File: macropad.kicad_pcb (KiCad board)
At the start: 2 copper layers, 13 parts, among them SW1 Rotary_Encoder_Switch, SW2 Rotary_Encoder_Switch, SW3 Rotary_Encoder_Switch, SW4 Rotary_Encoder_Switch, SW5 Rotary_Encoder_Switch, SW6 Rotary_Encoder_Switch, U1 ProMicro

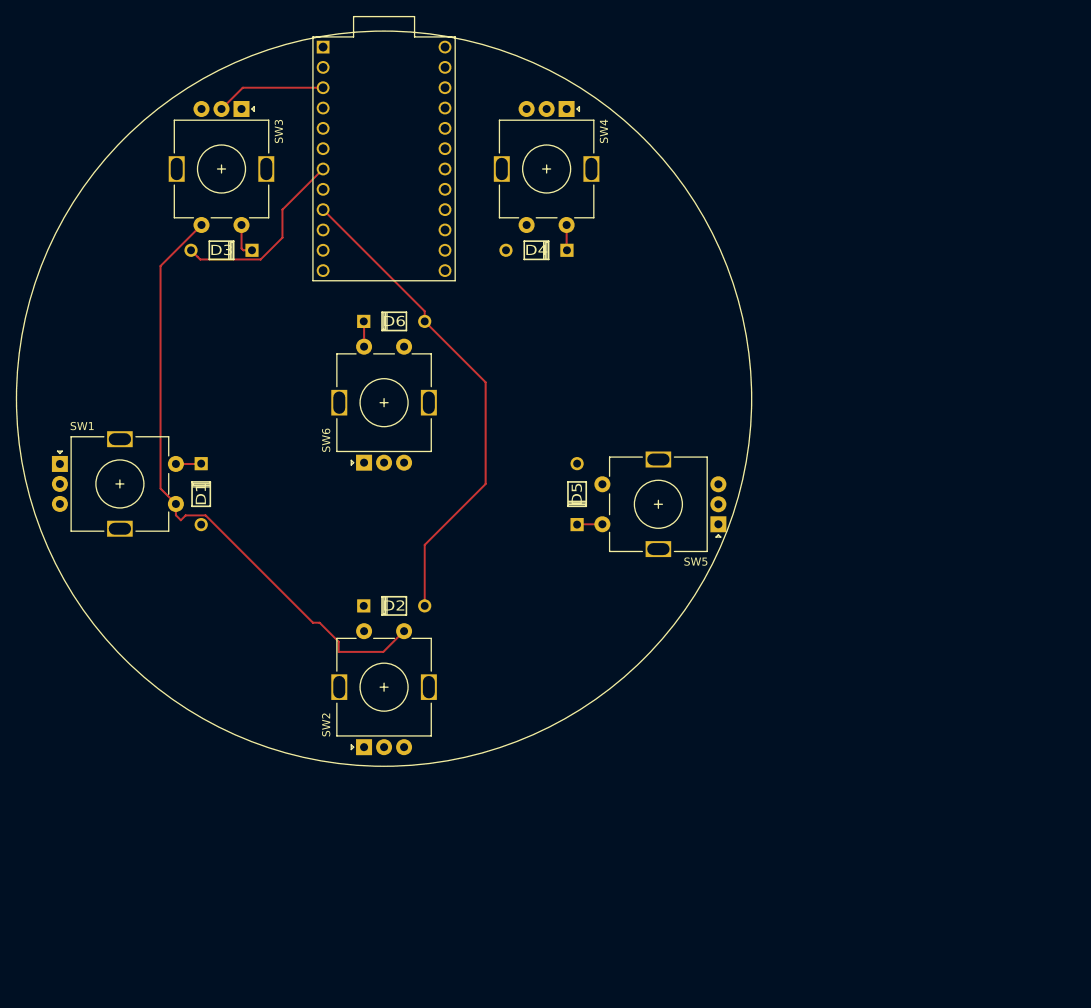
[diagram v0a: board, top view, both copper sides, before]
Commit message: moved to 70mm circle, just before routing
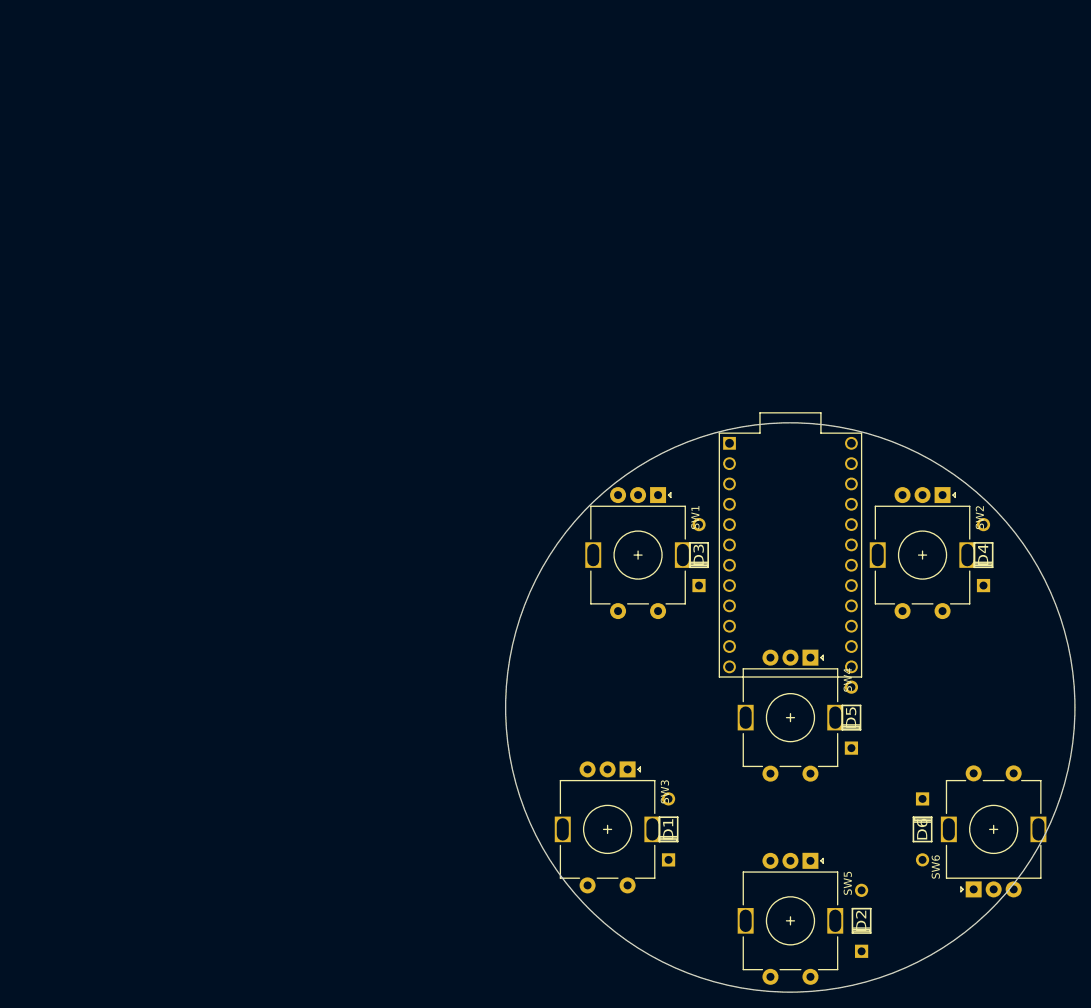
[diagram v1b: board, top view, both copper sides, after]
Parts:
- moved SW6 93.0 mm to (175.3, 118.1)
- moved D6 91.6 mm to (166.4, 118.1), turned to 90 degrees
- moved SW3 74.7 mm to (127.0, 118.1), turned to 270 degrees
- moved D1 71.9 mm to (134.6, 118.1), turned to 270 degrees
- moved SW1 71.0 mm to (130.8, 83.8)
- moved U1 70.9 mm to (149.9, 83.8)
- moved D3 70.8 mm to (138.4, 83.8), turned to 270 degrees
- moved D2 70.4 mm to (158.8, 129.5), turned to 270 degrees
- moved D4 67.6 mm to (174.0, 83.8), turned to 270 degrees
- moved SW2 67.4 mm to (166.4, 83.8)
- moved SW5 58.6 mm to (149.9, 129.5), turned to 270 degrees
- moved D5 44.2 mm to (157.5, 104.1)
- moved SW4 31.4 mm to (149.9, 104.1), turned to 270 degrees
- renumbered SW3 to SW1, SW4 to SW2, SW1 to SW3, SW5 to SW4, SW2 to SW5
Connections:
- U1 pad 1: RE4-0 -> RE0-0
- U1 pad 19: RE0-1 -> RE4-1
- U1 pad 2: RE4-1 -> RE0-1
- U1 pad 20: RE0-0 -> RE4-0
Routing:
- net Net-(SW1-PadS1): track 77.1 -> 0.00 mm
- net ROW2: track 61.1 -> 0.00 mm
- net ROW0: track 23.7 -> 0.00 mm
- net GND: track 13.8 -> 0.00 mm
- net Net-(D3-Pad2): track 4.33 -> 0.00 mm
- net Net-(D4-Pad2): track 3.18 -> 0.00 mm
- net Net-(D5-Pad2): track 3.18 -> 0.00 mm
- net Net-(D6-Pad2): track 3.18 -> 0.06 mm
- net Net-(D1-Pad2): track 3.18 -> 0.06 mm
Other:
- board outline added: 71.2 x 71.2 mm

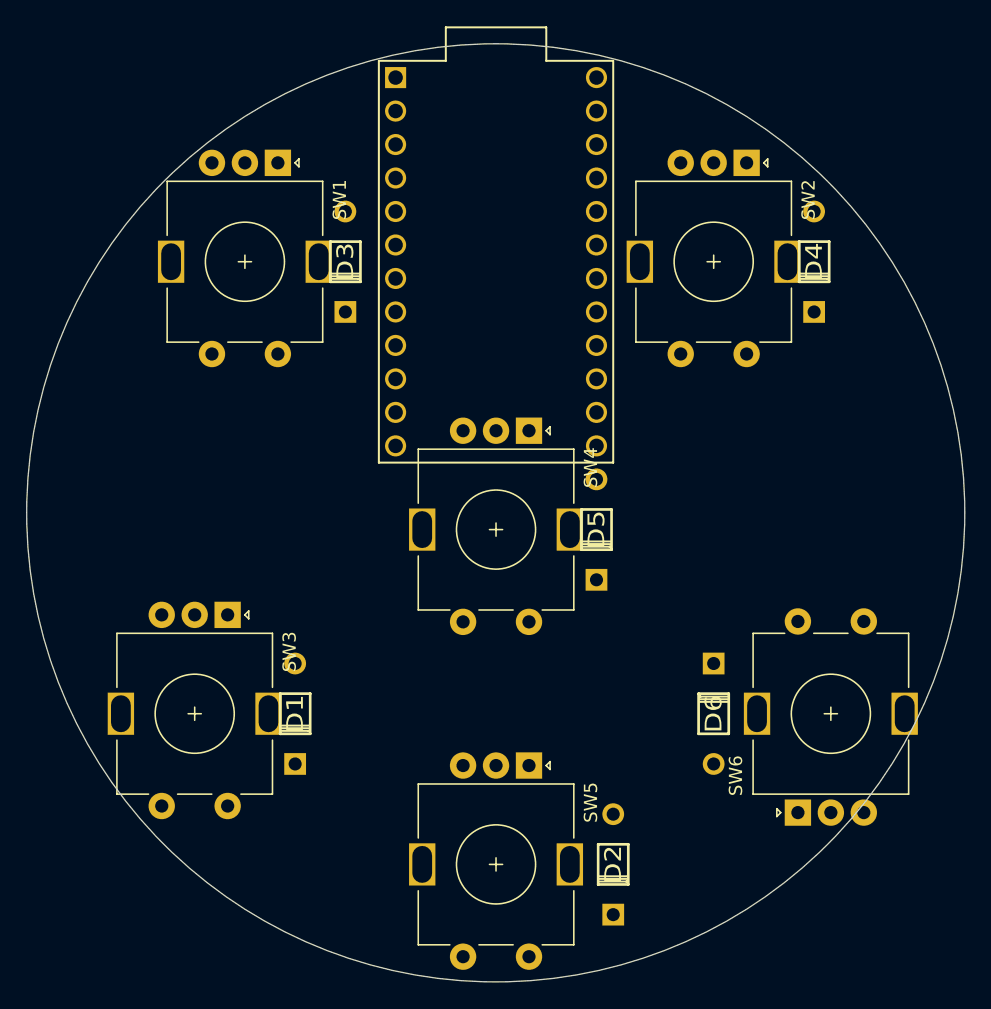
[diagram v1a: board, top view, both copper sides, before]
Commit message: finished first pass routing
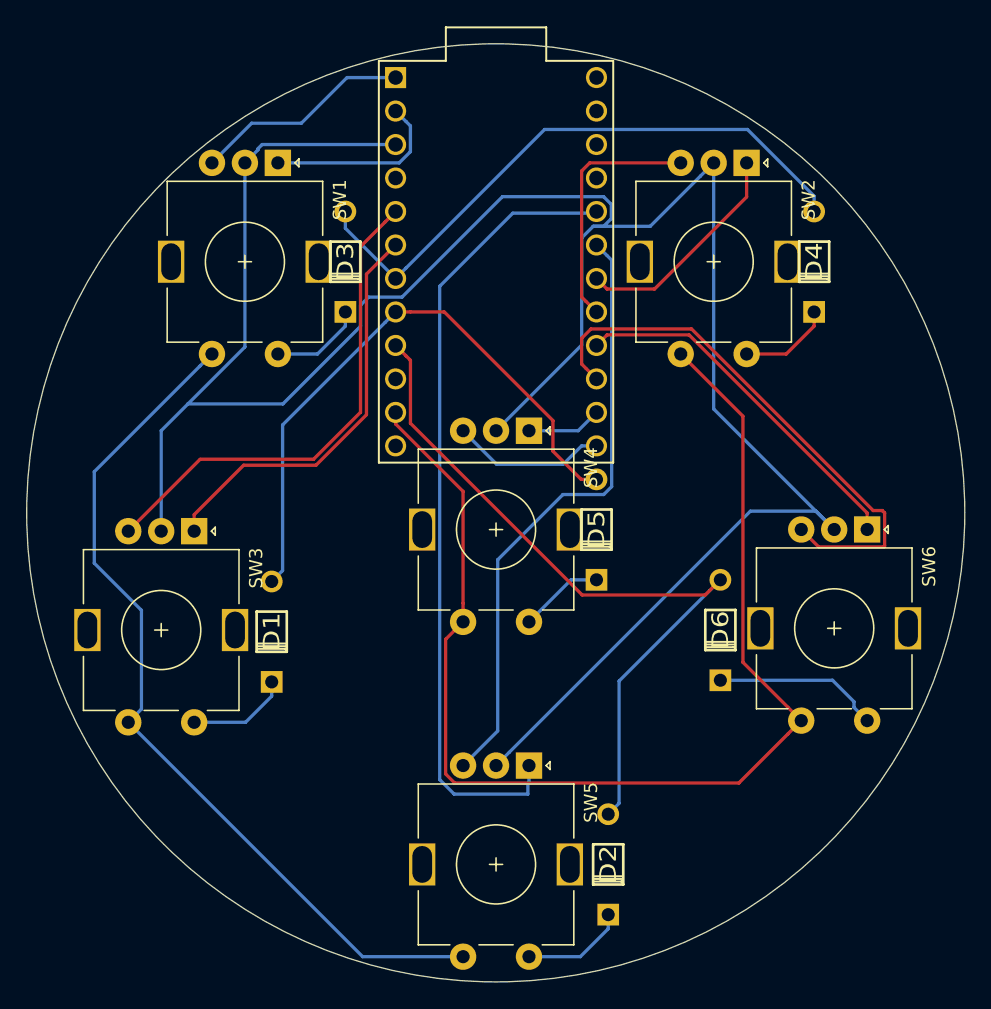
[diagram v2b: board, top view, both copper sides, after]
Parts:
- moved SW3 6.84 mm to (124.5, 111.8)
- moved SW6 6.48 mm to (175.5, 111.6), turned to 270 degrees
- moved D1 6.47 mm to (132.8, 111.9)
- moved D6 6.37 mm to (166.9, 111.8), turned to 270 degrees
- moved D2 0.38 mm to (158.4, 129.5)
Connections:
- SW1 pad A: RE0-0 -> RE0-1
- SW1 pad B: RE0-1 -> RE0-0
- SW3 pad A: RE2-0 -> RE5-1
- SW3 pad B: RE2-1 -> RE5-0
- SW6 pad A: RE5-0 -> RE2-0
- SW6 pad B: RE5-1 -> RE2-1
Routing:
- net GND: track 0.00 -> 180.7 mm
- net COL1: track 0.00 -> 90.9 mm
- net Net-(SW1-PadS1): track 0.00 -> 66.3 mm
- net RE4-0: track 0.00 -> 61.0 mm
- net ROW2: track 0.00 -> 57.1 mm
- net RE4-1: track 0.00 -> 46.4 mm
- net ROW0: track 0.00 -> 46.4 mm
- net ROW1: track 0.00 -> 46.2 mm
- net RE2-1: track 0.00 -> 42.0 mm
- net RE5-0: track 0.00 -> 37.7 mm
- net RE5-1: track 0.00 -> 31.3 mm
- net RE2-0: track 0.00 -> 27.7 mm
- net RE1-1: track 0.00 -> 18.9 mm
- net RE1-0: track 0.00 -> 17.2 mm
- net RE0-0: track 0.00 -> 16.6 mm
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
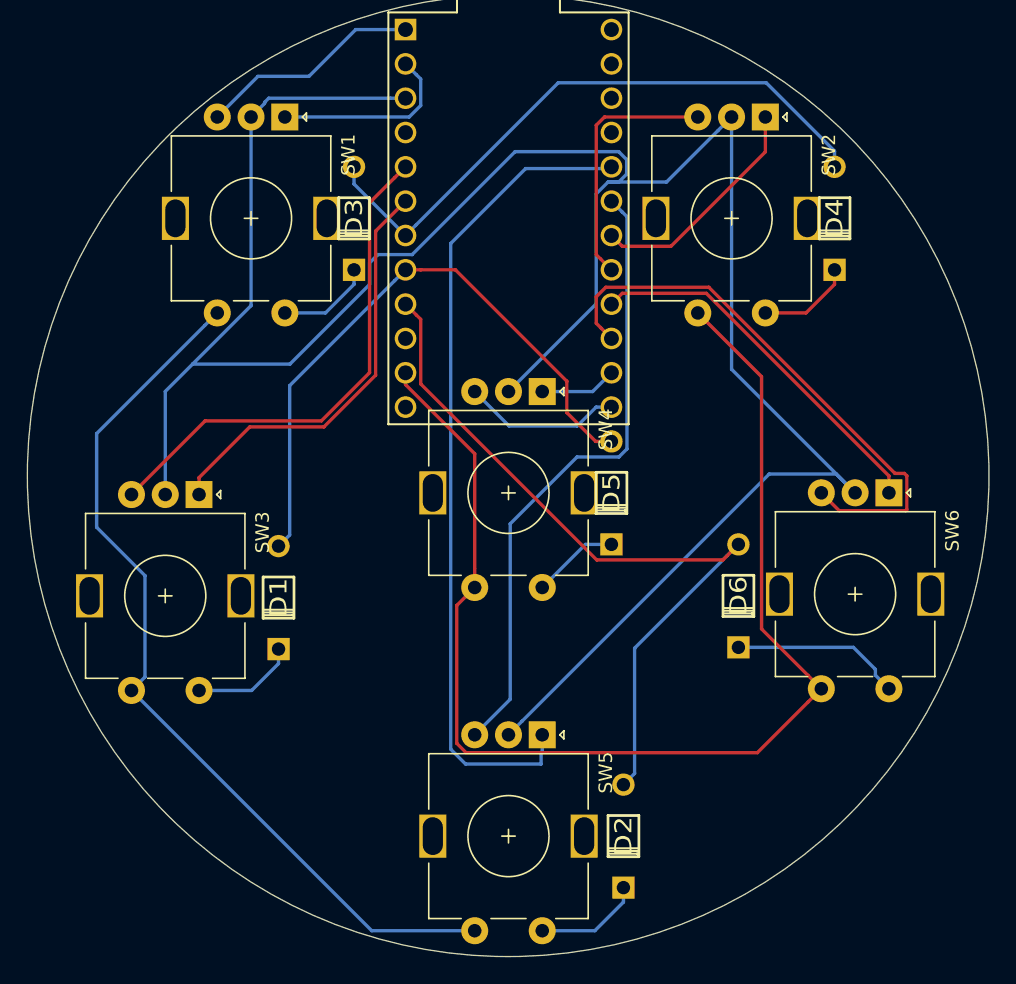
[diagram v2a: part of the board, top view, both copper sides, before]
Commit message: Created new footprint and fixed routing
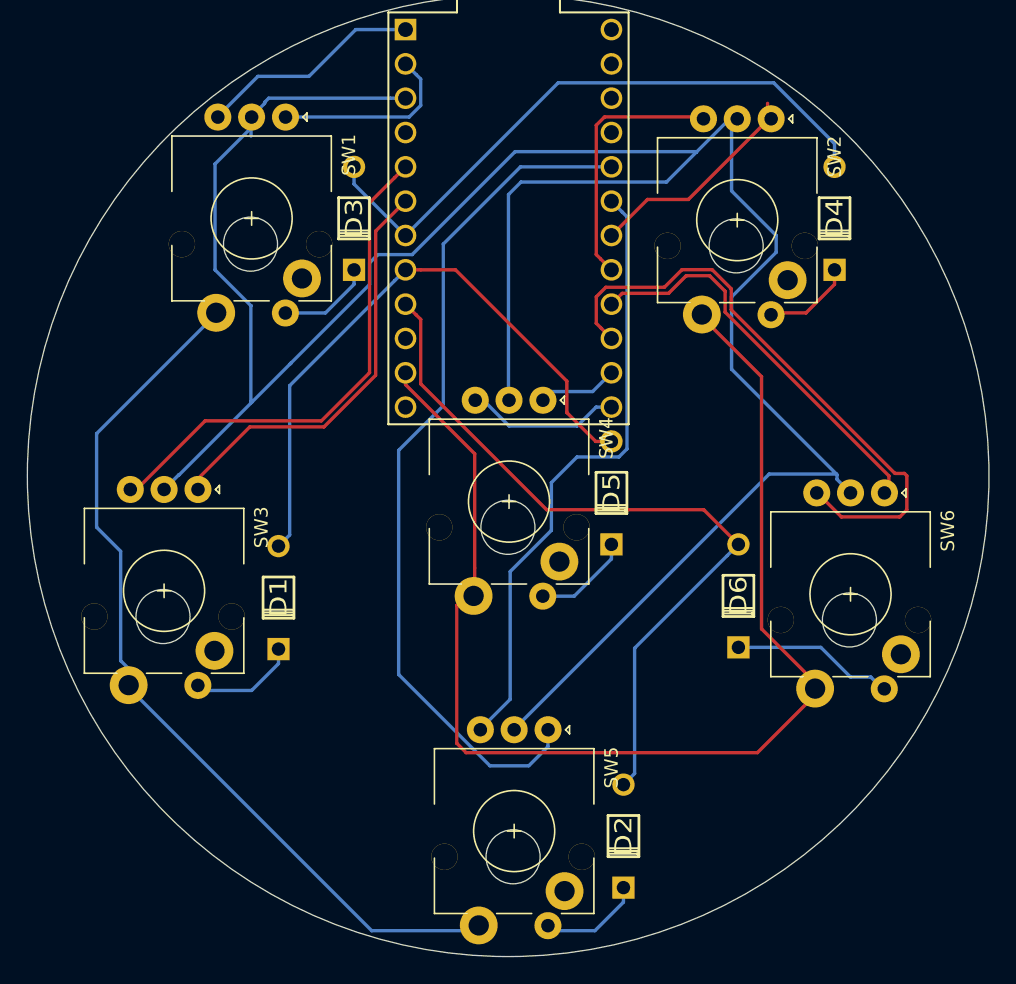
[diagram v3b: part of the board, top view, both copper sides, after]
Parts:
- SW1, SW2, SW3, SW4, SW5, SW6: footprint Keebio-Parts:RotaryEncoder_Alps_EC11E-Switch_Vertical_H20mm -> Rotary_Encoder:RotaryEncoder_MX
- moved SW5 8.40 mm to (152.8, 121.7)
- moved SW3 8.24 mm to (126.9, 103.9)
- moved SW2 7.92 mm to (169.3, 76.5)
- moved SW1 7.91 mm to (133.3, 76.3)
- moved SW6 7.80 mm to (177.7, 104.1)
- moved SW4 7.31 mm to (152.4, 97.3)
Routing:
- net GND: track 180.7 -> 186.8 mm
- net RE4-0: track 61.0 -> 63.7 mm
- net RE2-1: track 42.0 -> 44.7 mm
- net RE2-0: track 27.7 -> 29.7 mm
- net ROW0: track 46.4 -> 47.8 mm
- net ROW2: track 57.1 -> 56.1 mm
- net RE1-0: track 17.2 -> 16.3 mm
- net Net-(D5-Pad2): track 6.44 -> 7.30 mm
- net Net-(SW1-PadS1): track 66.3 -> 65.8 mm
- net Net-(D6-Pad2): track 12.7 -> 12.1 mm

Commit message: first print
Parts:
- added G***: LOGO, art:moon-phases, B.Cu at (149.8, 102.9)
- added G***: LOGO, art:star, F.Cu at (149.5, 106.7)
- added HOLE_M2: VAL**, Lily58-footprint:HOLE_M2, F.Cu at (161.4, 134.0)
- added HOLE_M2: VAL**, Lily58-footprint:HOLE_M2, F.Cu at (138.7, 134.0)
- added HOLE_M2: VAL**, Lily58-footprint:HOLE_M2, F.Cu at (116.4, 100.9)
- added HOLE_M2: VAL**, Lily58-footprint:HOLE_M2, F.Cu at (183.1, 100.9)
- added HOLE_M2: VAL**, Lily58-footprint:HOLE_M2, F.Cu at (138.6, 71.6)
- added HOLE_M2: VAL**, Lily58-footprint:HOLE_M2, F.Cu at (161.3, 71.6)
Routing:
- net RE0-0: track 16.6 -> 18.4 mm
